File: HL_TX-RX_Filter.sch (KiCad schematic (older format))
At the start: 210 parts, among them J1 CNR1, J10 SCL SDA, J11 To Rx in, J12 CONN_01X03, J2 CNR3, J3 Antenna, J4 CNR2, J5 CNR4, J6 From Tx, J7 + - 12v, J8 ICSP, J9 CONN_01X05, Q1 2N7002, Q2 2N7002, Q3 2N7002, Q4 2N7002, Q5 2N7002, Q6 2N7002, Q7 2N7002, Q8 2N7002, U1 ATMEGA328-AU, U10 PE4259, U11 PE4259, U12 PE4259, U2 PE4259, U3 PE4259, U4 PE4259, U5 PE4259, U6 PE4259, U7 PE4259, U8 PE4259, U9 PE4259

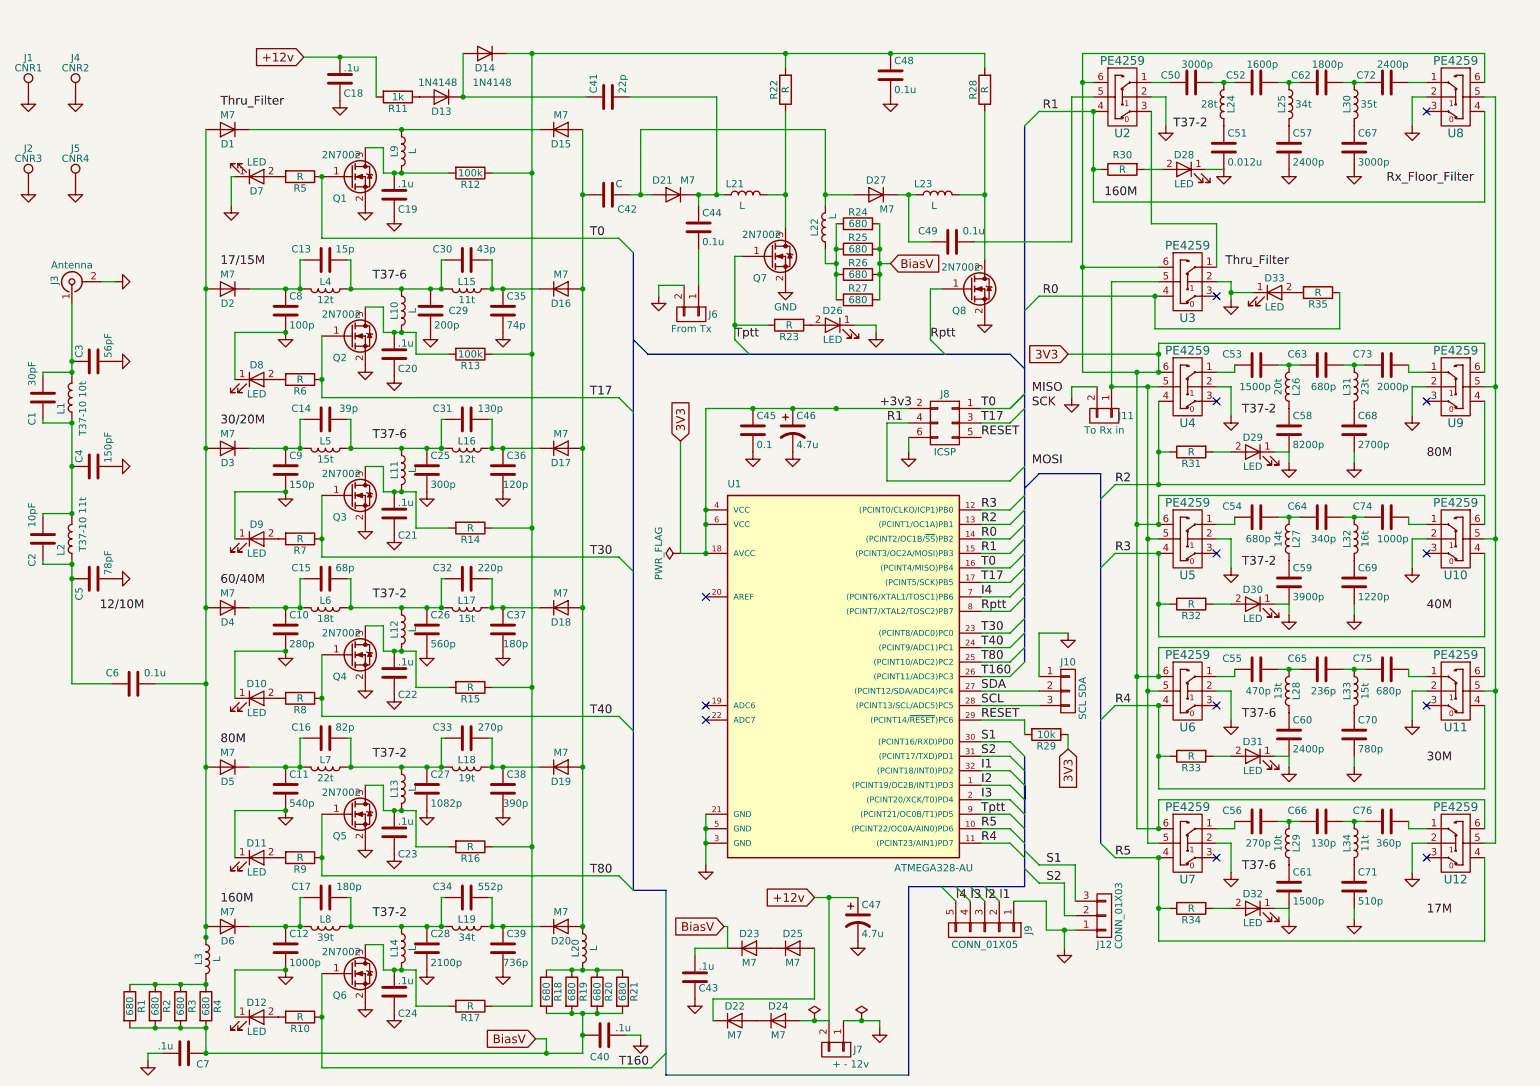
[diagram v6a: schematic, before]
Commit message: Terminated PE4259s and annotated more components
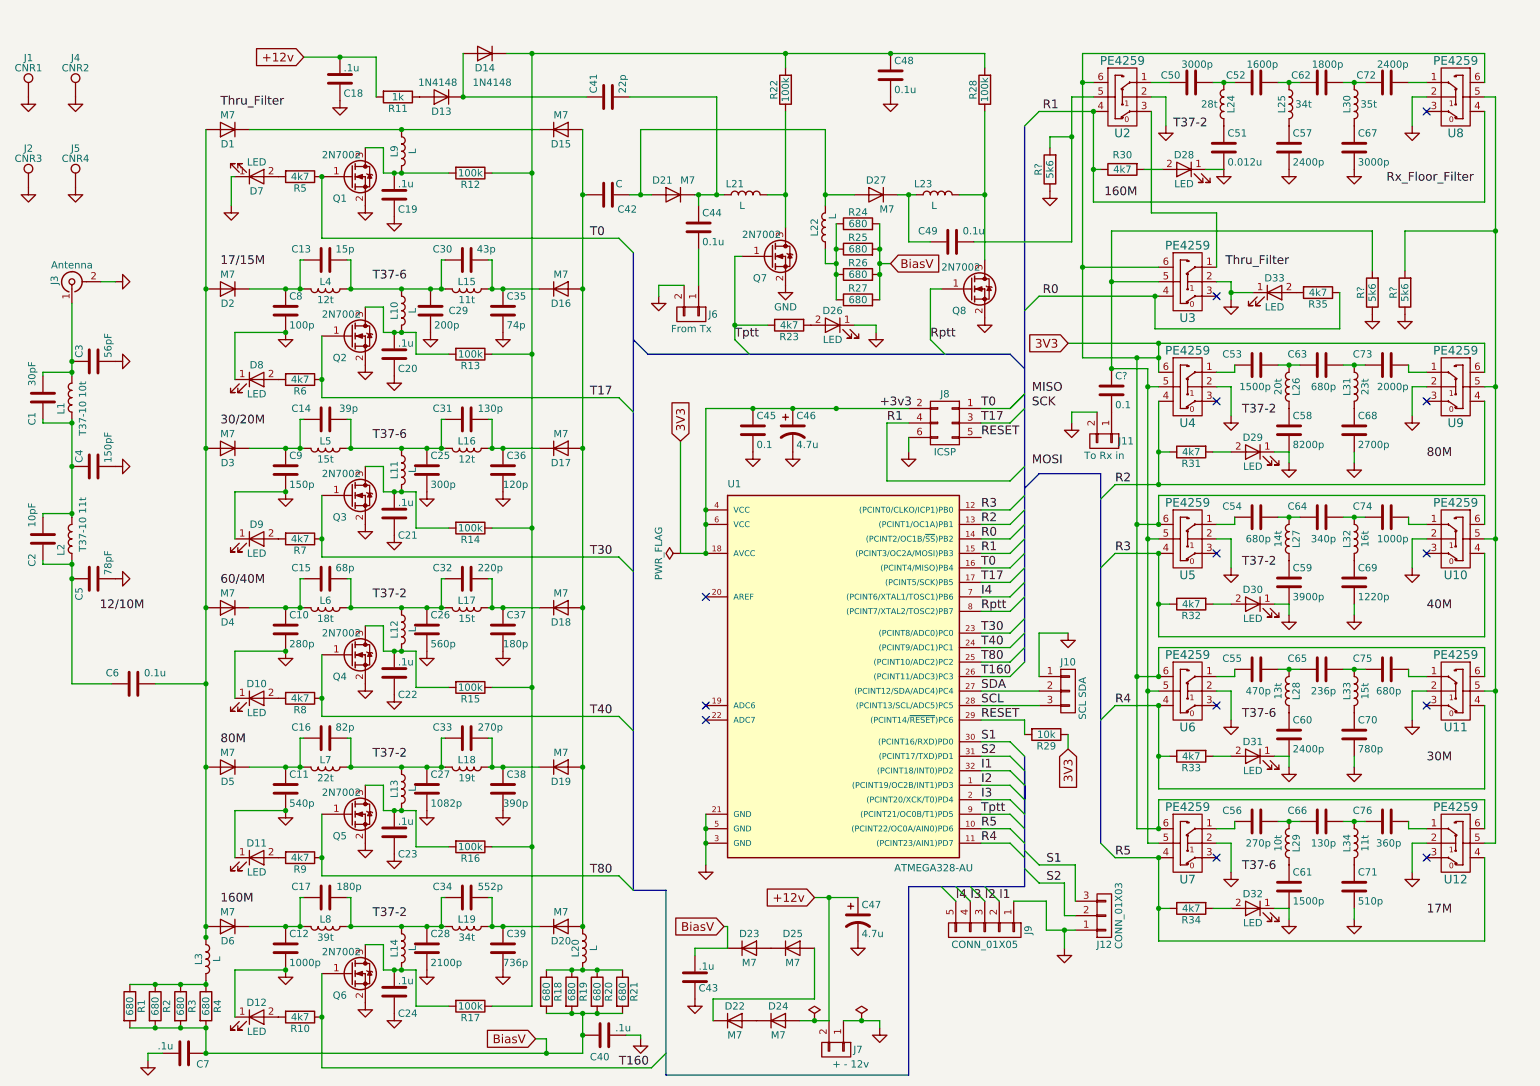
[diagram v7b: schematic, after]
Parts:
- added C?: 0.1, Capacitors_SMD:C_1206_HandSoldering, symbol C
- added R? (x3): 5k6, Resistors_SMD:R_1206_HandSoldering, symbol R
- R10, R23, R30, R31, R32, R33, R34, R35, R5, R6, R7, R8, R9: value R -> 4k7
- R14, R15, R16, R17, R22, R28: value R -> 100k
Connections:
- net GND: now also R?.1, R?.1, R?.1
- net at C49.2, U2.5: now also R?.2
- net at U10.5, U11.5, U12.5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: now also R?.2
- net at U3.5, U4.5, U5.5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: now also C?.1, R?.2; no longer J11.1 (P1)
- new net: C?.2, J11.1 (P1)
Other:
- moved on the sheet: J11
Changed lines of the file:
@@
 P 3775 7175
 F 0 "R17" V 3855 7175 50  0000 C CNN
-F 1 "R" V 3775 7175 50  0000 C CNN
+F 1 "100k" V 3775 7175 50  0000 C CNN
 F 2 "Resistors_SMD:R_1206_HandSoldering" V 3705 7175 50  0001 C CNN
 F 3 "" H 3775 7175 50  0001 C CNN
@@
 P 3775 6075
 F 0 "R16" V 3855 6075 50  0000 C CNN
-F 1 "R" V 3775 6075 50  0000 C CNN
+F 1 "100k" V 3775 6075 50  0000 C CNN
 F 2 "Resistors_SMD:R_1206_HandSoldering" V 3705 6075 50  0001 C CNN
 F 3 "" H 3775 6075 50  0001 C CNN
@@
 P 3775 4975
 F 0 "R15" V 3855 4975 50  0000 C CNN
-F 1 "R" V 3775 4975 50  0000 C CNN
+F 1 "100k" V 3775 4975 50  0000 C CNN
 F 2 "Resistors_SMD:R_1206_HandSoldering" V 3705 4975 50  0001 C CNN
 F 3 "" H 3775 4975 50  0001 C CNN
@@
 P 3775 3875
 F 0 "R14" V 3855 3875 50  0000 C CNN
-F 1 "R" V 3775 3875 50  0000 C CNN
+F 1 "100k" V 3775 3875 50  0000 C CNN
 F 2 "Resistors_SMD:R_1206_HandSoldering" V 3705 3875 50  0001 C CNN
 F 3 "" H 3775 3875 50  0001 C CNN
@@
 P 7325 850
 F 0 "R28" V 7405 850 50  0000 C CNN
-F 1 "R" V 7325 850 50  0000 C CNN
+F 1 "100k" V 7325 850 50  0000 C CNN
 F 2 "Resistors_SMD:R_1206_HandSoldering" V 7255 850 50  0001 C CNN
 F 3 "" H 7325 850 50  0001 C CNN
@@
 P 5950 850
 F 0 "R22" V 6030 850 50  0000 C CNN
-F 1 "R" V 5950 850 50  0000 C CNN
+F 1 "100k" V 5950 850 50  0000 C CNN
 F 2 "Resistors_SMD:R_1206_HandSoldering" V 5880 850 50  0001 C CNN
 F 3 "" H 5950 850 50  0001 C CNN
@@
 Text GLabel 6675 2050 2    60   Input ~ 0
 BiasV
-Text GLabel 7900 2675 0    60   Input ~ 0
+Text GLabel 7900 2600 0    60   Input ~ 0
 3V3
 Text Label 7725 2275 0    60   ~ 0
@@
 P 2600 6150
 F 0 "R9" V 2680 6150 50  0000 C CNN
-F 1 "R" V 2600 6150 50  0000 C CNN
+F 1 "4k7" V 2600 6150 50  0000 C CNN
 F 2 "Resistors_SMD:R_1206_HandSoldering" V 2530 6150 50  0001 C CNN
 F 3 "" H 2600 6150 50  0001 C CNN
@@
 P 2600 7250
 F 0 "R10" V 2680 7250 50  0000 C CNN
-F 1 "R" V 2600 7250 50  0000 C CNN
+F 1 "4k7" V 2600 7250 50  0000 C CNN
 F 2 "Resistors_SMD:R_1206_HandSoldering" V 2530 7250 50  0001 C CNN
 F 3 "" H 2600 7250 50  0001 C CNN
@@
 P 2600 5050
 F 0 "R8" V 2680 5050 50  0000 C CNN
-F 1 "R" V 2600 5050 50  0000 C CNN
+F 1 "4k7" V 2600 5050 50  0000 C CNN
 F 2 "Resistors_SMD:R_1206_HandSoldering" V 2530 5050 50  0001 C CNN
 F 3 "" H 2600 5050 50  0001 C CNN
@@
 P 2600 3950
 F 0 "R7" V 2680 3950 50  0000 C CNN
-F 1 "R" V 2600 3950 50  0000 C CNN
+F 1 "4k7" V 2600 3950 50  0000 C CNN
 F 2 "Resistors_SMD:R_1206_HandSoldering" V 2530 3950 50  0001 C CNN
 F 3 "" H 2600 3950 50  0001 C CNN
@@
 P 2600 2850
 F 0 "R6" V 2680 2850 50  0000 C CNN
-F 1 "R" V 2600 2850 50  0000 C CNN
+F 1 "4k7" V 2600 2850 50  0000 C CNN
 F 2 "Resistors_SMD:R_1206_HandSoldering" V 2530 2850 50  0001 C CNN
 F 3 "" H 2600 2850 50  0001 C CNN
@@
 P 2600 1450
 F 0 "R5" V 2680 1450 50  0000 C CNN
-F 1 "R" V 2600 1450 50  0000 C CNN
+F 1 "4k7" V 2600 1450 50  0000 C CNN
 F 2 "Resistors_SMD:R_1206_HandSoldering" V 2530 1450 50  0001 C CNN
 F 3 "" H 2600 1450 50  0001 C CNN
@@
 L CONN_01X02 J11
 U 1 1 596713D0
-P 8150 3100
-F 0 "J11" V 8150 3250 50  0000 C CNN
-F 1 "To Rx in" V 8250 3100 50  0000 C CNN
-F 2 "Pin_Headers:Pin_Header_Straight_1x02_Pitch2.54mm" H 8150 3100 50  0001 C CNN
-F 3 "" H 8150 3100 50  0001 C CNN
-	1    8150 3100
+P 8150 3275
+F 0 "J11" V 8150 3425 50  0000 C CNN
+F 1 "To Rx in" V 8250 3275 50  0000 C CNN
+F 2 "Pin_Headers:Pin_Header_Straight_1x02_Pitch2.54mm" H 8150 3275 50  0001 C CNN
+F 3 "" H 8150 3275 50  0001 C CNN
+	1    8150 3275
 	0    1    1    0
 $EndComp
@@
 L GND #PWR059
 U 1 1 596713D6
-P 7925 2975
-F 0 "#PWR059" H 7925 2725 50  0001 C CNN
-F 1 "GND" H 7925 2825 50  0001 C CNN
-F 2 "" H 7925 2975 50  0001 C CNN
-F 3 "" H 7925 2975 50  0001 C CNN
-	1    7925 2975
+P 7925 3150
+F 0 "#PWR059" H 7925 2900 50  0001 C CNN
+F 1 "GND" H 7925 3000 50  0001 C CNN
+F 2 "" H 7925 3150 50  0001 C CNN
+F 3 "" H 7925 3150 50  0001 C CNN
+	1    7925 3150
 	1    0    0    -1
 $EndComp
@@
 P 8750 3350
 F 0 "R31" V 8830 3350 50  0000 C CNN
-F 1 "R" V 8750 3350 50  0000 C CNN
+F 1 "4k7" V 8750 3350 50  0000 C CNN
 F 2 "Resistors_SMD:R_1206_HandSoldering" V 8680 3350 50  0001 C CNN
 F 3 "" H 8750 3350 50  0001 C CNN
@@
 P 8275 1400
 F 0 "R30" V 8175 1400 50  0000 C CNN
-F 1 "R" V 8275 1400 50  0000 C CNN
+F 1 "4k7" V 8275 1400 50  0000 C CNN
 F 2 "Resistors_SMD:R_1206_HandSoldering" V 8205 1400 50  0001 C CNN
 F 3 "" H 8275 1400 50  0001 C CNN
@@
 P 8750 4400
 F 0 "R32" V 8830 4400 50  0000 C CNN
-F 1 "R" V 8750 4400 50  0000 C CNN
+F 1 "4k7" V 8750 4400 50  0000 C CNN
 F 2 "Resistors_SMD:R_1206_HandSoldering" V 8680 4400 50  0001 C CNN
 F 3 "" H 8750 4400 50  0001 C CNN
@@
 P 8750 5450
 F 0 "R33" V 8830 5450 50  0000 C CNN
-F 1 "R" V 8750 5450 50  0000 C CNN
+F 1 "4k7" V 8750 5450 50  0000 C CNN
 F 2 "Resistors_SMD:R_1206_HandSoldering" V 8680 5450 50  0001 C CNN
 F 3 "" H 8750 5450 50  0001 C CNN
@@
 P 8750 6500
 F 0 "R34" V 8830 6500 50  0000 C CNN
-F 1 "R" V 8750 6500 50  0000 C CNN
+F 1 "4k7" V 8750 6500 50  0000 C CNN
 F 2 "Resistors_SMD:R_1206_HandSoldering" V 8680 6500 50  0001 C CNN
 F 3 "" H 8750 6500 50  0001 C CNN
@@
 P 9625 2250
 F 0 "R35" V 9705 2250 50  0000 C CNN
-F 1 "R" V 9625 2250 50  0000 C CNN
+F 1 "4k7" V 9625 2250 50  0000 C CNN
 F 2 "Resistors_SMD:R_1206_HandSoldering" V 9555 2250 50  0001 C CNN
 F 3 "" H 9625 2250 50  0001 C CNN
@@
 P 5975 2475
 F 0 "R23" V 6055 2475 50  0000 C CNN
-F 1 "R" V 5975 2475 50  0000 C CNN
+F 1 "4k7" V 5975 2475 50  0000 C CNN
 F 2 "Resistors_SMD:R_1206_HandSoldering" V 5905 2475 50  0001 C CNN
 F 3 "" H 5975 2475 50  0001 C CNN
@@
 	10775 3575 10775 3000
 Wire Wire Line
-	8525 2800 8525 2600
+	8525 2600 8525 2800
 Wire Wire Line
-	8525 2600 10775 2600
+	7900 2600 10775 2600
 Wire Wire Line
 	10775 2600 10775 2800
@@
 	8075 800  8000 800
 Wire Wire Line
-	8000 600  8000 2800
+	8000 600  8000 2700
 Wire Wire Line
-	8000 2800 8525 2800
+	8000 2700 8525 2700
 Wire Wire Line
 	8450 3950 8525 3950
@@
 	7925 900  7925 1900
 Wire Wire Line
-	8200 2900 8525 2900
+	8200 2775 8450 2775
 Wire Wire Line
 	10850 6050 10775 6050
@@
 	10775 5000 10850 5000
 Connection ~ 10850 5000
-Connection ~ 8375 2800
+Connection ~ 8375 2700
 Connection ~ 8450 2900
 Wire Wire Line
-	8450 2900 8450 6050
+	8450 2775 8450 6050
 Wire Wire Line
-	8375 2800 8375 5950
+	8375 2700 8375 5950
 Wire Wire Line
-	8925 2075 8925 1775
+	8925 2075 8925 1700
 Wire Wire Line
 	7300 5550 7500 5550
@@
 	4950 1125 4950 1575
 Connection ~ 4950 1575
-Wire Wire Line
-	7900 2675 8525 2675
-Connection ~ 8525 2675
+Connection ~ 8525 2600
 Wire Wire Line
 	8000 600  10775 600
@@
 	5075 2200 5075 2275
 Wire Wire Line
-	8100 2900 7925 2900
+	8100 3075 7925 3075
 Wire Wire Line
-	7925 2900 7925 2975
+	7925 3075 7925 3150
 Wire Wire Line
-	8200 2900 8200 2175
-Connection ~ 8200 2900
+	8200 1825 8200 2775
 Wire Wire Line
 	7925 1900 7250 1900
 Wire Wire Line
-	8925 1775 8475 1775
+	8925 1700 8475 1700
 Wire Wire Line
-	8475 1775 8475 1000
+	8475 1700 8475 1000
 Wire Wire Line
 	8200 2175 8525 2175
@@
 Connection ~ 8525 4050
 Connection ~ 8525 3850
-Connection ~ 8525 2800
+Connection ~ 8525 2700
 Wire Wire Line
 	3400 2525 3400 2675
@@
 Text Label 9100 6250 0    60   ~ 0
 T37-6
+Wire Wire Line
+	8525 2900 8450 2900
+$Comp
+L C C?
+U 1 1 59F5F3C8
+P 8200 2925
+F 0 "C?" H 8225 3025 50  0000 L CNN
+F 1 "0.1" H 8225 2825 50  0000 L CNN
+F 2 "Capacitors_SMD:C_1206_HandSoldering" H 8238 2775 50  0001 C CNN
+F 3 "" H 8200 2925 50  0001 C CNN
+	1    8200 2925
+	1    0    0    -1
+$EndComp
+Connection ~ 8200 2775
+$Comp
+L R R?
+U 1 1 59F61CEF
+P 7775 1400
+F 0 "R?" V 7855 1400 50  0000 C CNN
+F 1 "5k6" V 7775 1400 50  0000 C CNN
+F 2 "Resistors_SMD:R_1206_HandSoldering" V 7705 1400 50  0001 C CNN
+F 3 "" H 7775 1400 50  0001 C CNN
+	1    7775 1400
+	-1   0    0    1
+$EndComp
+Wire Wire Line
+	7775 1250 7775 1175
+Wire Wire Line
+	7775 1175 7925 1175
+Connection ~ 7925 1175
+$Comp
+L GND #PWR?
+U 1 1 59F62A3F
+P 7775 1550
+F 0 "#PWR?" H 7775 1300 50  0001 C CNN
+F 1 "GND" H 7775 1400 50  0001 C CNN
+F 2 "" H 7775 1550 50  0001 C CNN
+F 3 "" H 7775 1550 50  0001 C CNN
+	1    7775 1550
+	1    0    0    -1
+$EndComp
+$Comp
+L R R?
+U 1 1 59F651B5
+P 10000 2250
+F 0 "R?" V 10080 2250 50  0000 C CNN
+F 1 "5k6" V 10000 2250 50  0000 C CNN
+F 2 "Resistors_SMD:R_1206_HandSoldering" V 9930 2250 50  0001 C CNN
+F 3 "" H 10000 2250 50  0001 C CNN
+	1    10000 2250
+	-1   0    0    1
+$EndComp
+Wire Wire Line
+	10000 1825 10000 2100
+$Comp
+L GND #PWR?
+U 1 1 59F651BC
+P 10000 2400
+F 0 "#PWR?" H 10000 2150 50  0001 C CNN
+F 1 "GND" H 10000 2250 50  0001 C CNN
+F 2 "" H 10000 2400 50  0001 C CNN
+F 3 "" H 10000 2400 50  0001 C CNN
+	1    10000 2400
+	1    0    0    -1
+$EndComp
+Wire Wire Line
+	10000 1825 8200 1825
+Connection ~ 8200 2175
+$Comp
+L R R?
+U 1 1 59F679A6
+P 10225 2250
+F 0 "R?" V 10305 2250 50  0000 C CNN
+F 1 "5k6" V 10225 2250 50  0000 C CNN
+F 2 "Resistors_SMD:R_1206_HandSoldering" V 10155 2250 50  0001 C CNN
+F 3 "" H 10225 2250 50  0001 C CNN
+	1    10225 2250
+	-1   0    0    1
+$EndComp
+Wire Wire Line
+	10225 1825 10225 2100
+$Comp
+L GND #PWR?
+U 1 1 59F679AD
+P 10225 2400
+F 0 "#PWR?" H 10225 2150 50  0001 C CNN
+F 1 "GND" H 10225 2250 50  0001 C CNN
+F 2 "" H 10225 2400 50  0001 C CNN
+F 3 "" H 10225 2400 50  0001 C CNN
+	1    10225 2400
+	1    0    0    -1
+$EndComp
+Wire Wire Line
+	10225 1825 10850 1825
+Connection ~ 10850 1825
 $EndSCHEMATC

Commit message: Rearrange filters
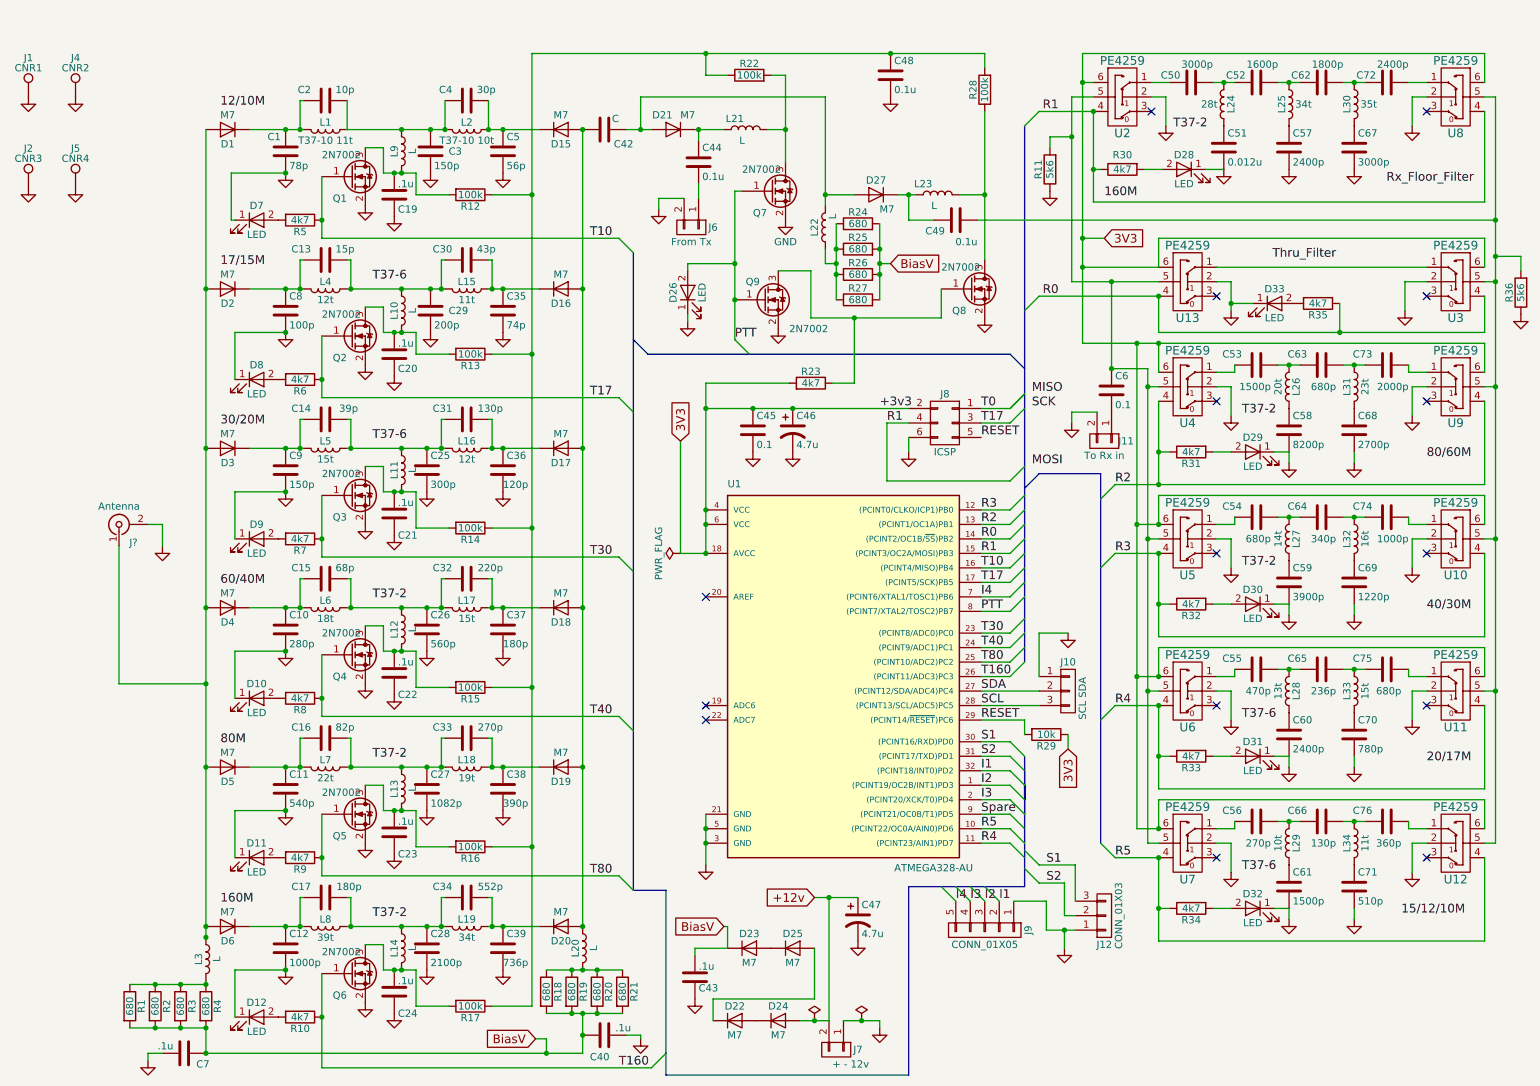
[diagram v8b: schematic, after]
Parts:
- removed C18: .1u, Capacitors_SMD:C_1206_HandSoldering, symbol C
- removed C41: 22p, Capacitors_SMD:C_1206_HandSoldering, symbol C
- removed C6: 0.1u, Capacitors_SMD:C_1206_HandSoldering, symbol C
- removed D13, D14: 1N4148, Diodes_SMD:D_MiniMELF_Handsoldering, symbol D
- removed J3: Antenna, Connectors_G:SMAEDGE_TH, symbol CONN_COAXIAL
- removed R11: 1k, Resistors_SMD:R_1206_HandSoldering, symbol R
- removed R?: 5k6, Resistors_SMD:R_1206_HandSoldering, symbol R
- added J?: Antenna, symbol Conn_Coaxial
- added Q9: 2N7002, TO_SOT_Packages_SMD:SOT-23, symbol Q_NMOS_GSD
- added U13: PE4259, TO_SOT_Packages_SMD:SOT-363_SC-70-6_Handsoldering, symbol PE4259
- C1: value 30pF -> 78p
- C2: value 10pF -> 10p
- C3: value 56pF -> 150p
- C4: value 150pF -> 30p
- C5: value 78pF -> 56p
- L1: value T37-10 10t -> T37-10 11t
- L2: value T37-10 11t -> T37-10 10t
- gave numbers to parts that had none: 3
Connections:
- net 3V3: now also R23.2, U13.6
- net GND: now also C1.2, J?.2 (Ext), Q9.2 (S), U13.2; no longer C4.2
- net R0: now also U13.4
- net T0: no longer Q1.1 (G), R5.1, U1.16 ((PCINT4/MISO)PB4)
- net at U2.3: no longer U3.1
- net at R11.2, U2.5: now also C6.1, U4.5, U5.5, U6.5, U7.5, U13.5; no longer C49.2
- net at R36.2, U10.5, U11.5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: now also C49.2, U3.5
- net at C48.1, R12.1, R13.1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: now also R22.1; no longer R22.2
- net at D1.2 (A), D2.2 (A), D3.2 (A)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: now also J?.1 (In)
- net at C2.2, C4.1, L1.1: now also C3.1, L2.1, L9.1; no longer C1.1, L2.2
- net at L21.2, Q7.3 (D): now also R22.2; no longer R22.1
- net PTT: now reaches D26.2 (A)
- net PTT: now also Q7.1 (G), U1.8 ((PCINT7/XTAL2/TOSC2)PB7), Q9.1 (G); no longer R23.2
- net Rptt: no longer names the net of Q8.1 (G)
- net Rptt: now also R23.1, Q9.3 (D); no longer U1.8 ((PCINT7/XTAL2/TOSC2)PB7)
- removed net Tptt: Q7.1 (G), R23.1, U1.9 ((PCINT21/OC0B/T1)PD5)
- new net: C4.2, C5.1, D15.1 (K), L2.2
- new net: C1.1, C2.1, D1.1 (K), L1.2
- new net: U13.1, U3.1
- new net Spare: U1.9 ((PCINT21/OC0B/T1)PD5)
- new net T10: Q1.1 (G), R5.1, U1.16 ((PCINT4/MISO)PB4)
- no-connect marks 13 -> 15
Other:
- moved on the sheet: C42, C44, C49, D21, D26, D33, D7, J6, L21, Q7, R12, R22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
